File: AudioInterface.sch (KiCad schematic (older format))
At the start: 2 parts, among them J3 Conn_01x03_Male

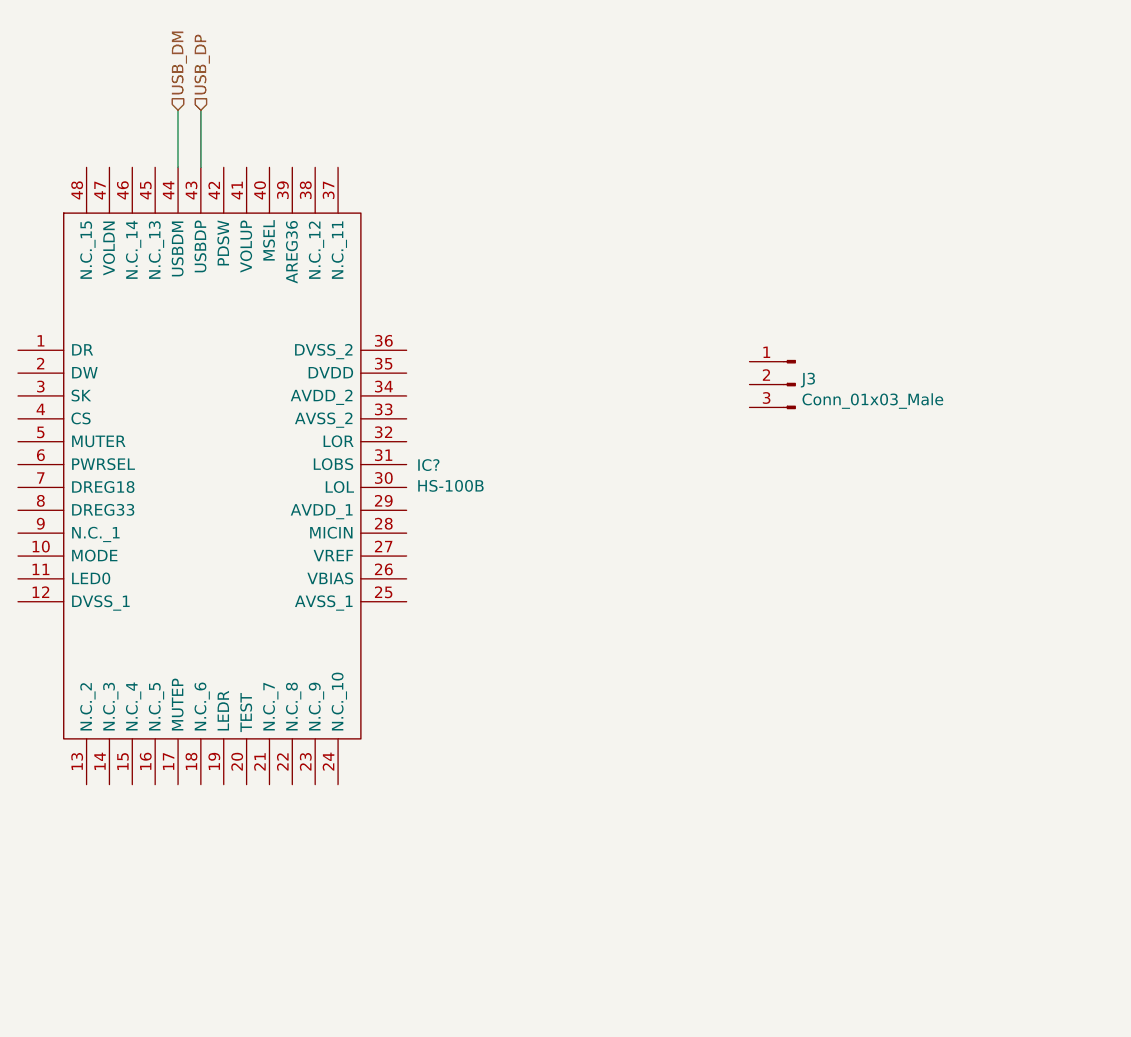
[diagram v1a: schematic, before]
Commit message: First pass at audio
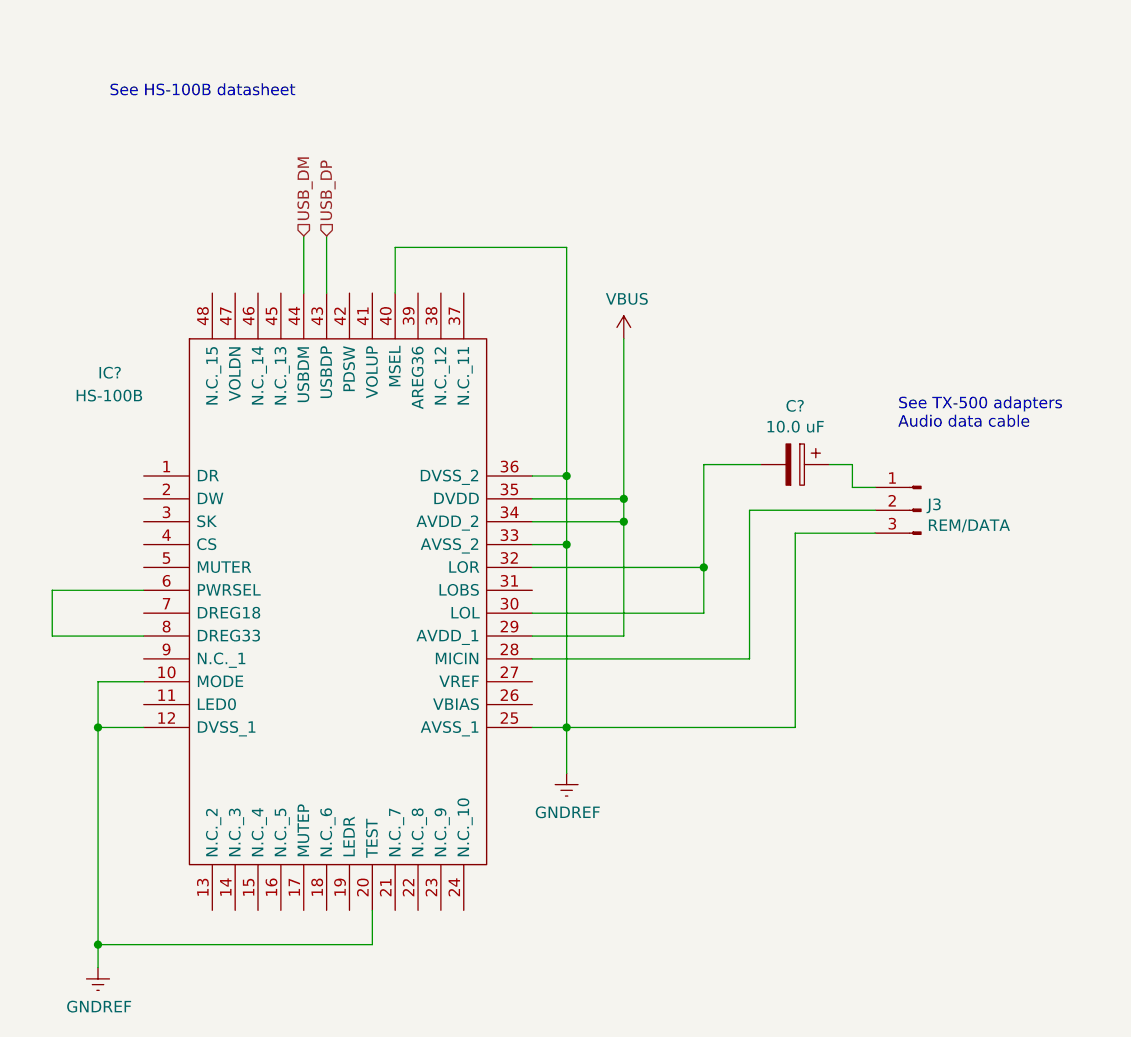
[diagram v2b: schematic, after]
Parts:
- added C?: 10.0 uF, symbol Device:CP
- J3: value Conn_01x03_Male -> REM/DATA
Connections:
- net GNDREF: now reaches IC?.10 (MODE)
- net GNDREF: now also IC?.12 (DVSS_1), IC?.20 (TEST), IC?.25 (AVSS_1), IC?.33 (AVSS_2), IC?.36 (DVSS_2), IC?.40 (MSEL), J3.3 (Pin_3)
- net at IC?.28 (MICIN): now also J3.2 (Pin_2)
- net VBUS: now reaches IC?.29 (AVDD_1)
- net VBUS: now also IC?.34 (AVDD_2), IC?.35 (DVDD)
- net at IC?.30 (LOL): now also IC?.32 (LOR), C?.2
- net at IC?.6 (PWRSEL): now also IC?.8 (DREG33)
- net at J3.1 (Pin_1): now also C?.1
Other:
- note added: "See HS-100B datasheet"
- note added: "See TX-500 adapters\nAudio data cable"
- moved on the sheet: IC?, J3
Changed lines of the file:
@@
 $Descr A4 11693 8268
 encoding utf-8
-Sheet 4 6
+Sheet 3 6
 Title ""
 Date ""
@@
 L HS-100B:HS-100B IC?
 U 1 1 605AF753
-P 4250 2800
+P 4800 3350
 AR Path="/605AF753" Ref="IC?"  Part="1"
 AR Path="/605AB33C/605AF753" Ref="IC?"  Part="1"
-F 0 "IC?" H 5994 2296 50  0000 L CNN
-F 1 "HS-100B" H 5994 2205 50  0000 L CNN
-F 2 "QFP50P900X900X160-48N" H 5800 3400 50  0001 L CNN
-F 3 "https://datasheet.lcsc.com/szlcsc/1906061502_Cmedia-HS-100B_C371351.pdf" H 5800 3300 50  0001 L CNN
-F 4 "LQFP-48 Video-Audio Interface ICs RoHS" H 5800 3200 50  0001 L CNN "Description"
-F 5 "1.6" H 5800 3100 50  0001 L CNN "Height"
-F 6 "cmedia" H 5800 3000 50  0001 L CNN "Manufacturer_Name"
-F 7 "HS-100B" H 5800 2900 50  0001 L CNN "Manufacturer_Part_Number"
-F 8 "" H 5800 2800 50  0001 L CNN "Mouser Part Number"
-F 9 "" H 5800 2700 50  0001 L CNN "Mouser Price/Stock"
-F 10 "" H 5800 2600 50  0001 L CNN "Arrow Part Number"
-F 11 "" H 5800 2500 50  0001 L CNN "Arrow Price/Stock"
-	1    4250 2800
+F 0 "IC?" H 4600 3800 50  0000 L CNN
+F 1 "HS-100B" H 4500 3700 50  0000 L CNN
+F 2 "QFP50P900X900X160-48N" H 6350 3950 50  0001 L CNN
+F 3 "https://datasheet.lcsc.com/szlcsc/1906061502_Cmedia-HS-100B_C371351.pdf" H 6350 3850 50  0001 L CNN
+F 4 "LQFP-48 Video-Audio Interface ICs RoHS" H 6350 3750 50  0001 L CNN "Description"
+F 5 "1.6" H 6350 3650 50  0001 L CNN "Height"
+F 6 "cmedia" H 6350 3550 50  0001 L CNN "Manufacturer_Name"
+F 7 "HS-100B" H 6350 3450 50  0001 L CNN "Manufacturer_Part_Number"
+F 8 "" H 6350 3350 50  0001 L CNN "Mouser Part Number"
+F 9 "" H 6350 3250 50  0001 L CNN "Mouser Price/Stock"
+F 10 "" H 6350 3150 50  0001 L CNN "Arrow Part Number"
+F 11 "" H 6350 3050 50  0001 L CNN "Arrow Price/Stock"
+	1    4800 3350
 	1    0    0    -1
 $EndComp
@@
 L Connector:Conn_01x03_Male J?
 U 1 1 605AF759
-P 7650 2950
+P 8200 3500
 AR Path="/605AF759" Ref="J?"  Part="1"
 AR Path="/605AB33C/605AF759" Ref="J3"  Part="1"
-F 0 "J3" H 7622 2974 50  0000 R CNN
-F 1 "Conn_01x03_Male" H 7622 2883 50  0000 R CNN
-F 2 "" H 7650 2950 50  0001 C CNN
-F 3 "~" H 7650 2950 50  0001 C CNN
-	1    7650 2950
+F 0 "J3" H 8172 3524 50  0000 R CNN
+F 1 "REM/DATA" H 8172 3433 50  0000 R CNN
+F 2 "" H 8200 3500 50  0001 C CNN
+F 3 "~" H 8200 3500 50  0001 C CNN
+	1    8200 3500
 	-1   0    0    -1
 $EndComp
-Text HLabel 5050 1750 1    50   Input ~ 0
+Text HLabel 5600 2300 1    50   Input ~ 0
 USB_DP
-Text HLabel 4950 1750 1    50   Input ~ 0
+Text HLabel 5500 2300 1    50   Input ~ 0
 USB_DM
 Wire Wire Line
-	5050 1750 5050 2000
+	5600 2300 5600 2550
 Wire Wire Line
-	4950 1750 4950 2000
+	5500 2300 5500 2550
+$Comp
+L power:GNDREF #PWR?
+U 1 1 604B503B
+P 6650 4650
+F 0 "#PWR?" H 6650 4400 50  0001 C CNN
+F 1 "GNDREF" H 6655 4477 50  0000 C CNN
+F 2 "" H 6650 4650 50  0001 C CNN
+F 3 "" H 6650 4650 50  0001 C CNN
+	1    6650 4650
+	1    0    0    -1
+$EndComp
+Wire Wire Line
+	6500 3350 6650 3350
+Wire Wire Line
+	6650 3350 6650 3650
+Wire Wire Line
+	6500 3650 6650 3650
+Connection ~ 6650 3650
+Wire Wire Line
+	6650 3650 6650 4450
+Wire Wire Line
+	6500 4450 6650 4450
+Connection ~ 6650 4450
+Wire Wire Line
+	6650 4450 6650 4650
+$Comp
+L power:GNDREF #PWR?
+U 1 1 604B77F8
+P 4600 5500
+F 0 "#PWR?" H 4600 5250 50  0001 C CNN
+F 1 "GNDREF" H 4605 5327 50  0000 C CNN
+F 2 "" H 4600 5500 50  0001 C CNN
+F 3 "" H 4600 5500 50  0001 C CNN
+	1    4600 5500
+	1    0    0    -1
+$EndComp
+Wire Wire Line
+	4800 4450 4600 4450
+Wire Wire Line
+	6500 4150 7450 4150
+Wire Wire Line
+	7450 4150 7450 3500
+Wire Wire Line
+	7450 3500 8000 3500
+Wire Wire Line
+	6500 3950 7250 3950
+Wire Wire Line
+	7250 3950 7250 3750
+Wire Wire Line
+	6500 3750 7250 3750
+Connection ~ 7250 3750
+$Comp
+L power:VBUS #PWR?
+U 1 1 604B97A3
+P 6900 2750
+F 0 "#PWR?" H 6900 2600 50  0001 C CNN
+F 1 "VBUS" H 6915 2923 50  0000 C CNN
+F 2 "" H 6900 2750 50  0001 C CNN
+F 3 "" H 6900 2750 50  0001 C CNN
+	1    6900 2750
+	1    0    0    -1
+$EndComp
+Wire Wire Line
+	6500 3450 6900 3450
+Wire Wire Line
+	6900 3450 6900 2750
+Wire Wire Line
+	6500 3550 6900 3550
+Wire Wire Line
+	6900 3550 6900 3450
+Connection ~ 6900 3450
+Wire Wire Line
+	6500 4050 6900 4050
+Wire Wire Line
+	6900 4050 6900 3550
+Connection ~ 6900 3550
+Wire Wire Line
+	5800 5250 5800 5400
+Wire Wire Line
+	5800 5400 4600 5400
+Wire Wire Line
+	4600 4450 4600 5400
+Wire Wire Line
+	4600 5400 4600 5500
+Connection ~ 4600 5400
+Wire Wire Line
+	4800 4250 4600 4250
+Wire Wire Line
+	4600 4250 4600 4450
+Connection ~ 4600 4450
+Wire Wire Line
+	4800 4050 4400 4050
+Wire Wire Line
+	4400 4050 4400 3850
+Wire Wire Line
+	4400 3850 4800 3850
+Wire Wire Line
+	5900 2550 5900 2350
+Wire Wire Line
+	5900 2350 6650 2350
+Wire Wire Line
+	6650 2350 6650 3350
+Connection ~ 6650 3350
+Text Notes 4650 1700 0    50   ~ 0
+See HS-100B datasheet
+Text Notes 8100 3150 0    50   ~ 0
+See TX-500 adapters\nAudio data cable
+$Comp
+L Device:CP C?
+U 1 1 604CC1E1
+P 7650 3300
+F 0 "C?" V 7395 3300 50  0000 C CNN
+F 1 "10.0 uF" V 7486 3300 50  0000 C CNN
+F 2 "" H 7688 3150 50  0001 C CNN
+F 3 "~" H 7650 3300 50  0001 C CNN
+	1    7650 3300
+	0    1    1    0
+$EndComp
+Wire Wire Line
+	7250 3300 7500 3300
+Wire Wire Line
+	7250 3300 7250 3750
+Wire Wire Line
+	7800 3300 7900 3300
+Wire Wire Line
+	7900 3300 7900 3400
+Wire Wire Line
+	7900 3400 8000 3400
+Wire Wire Line
+	8000 3600 7650 3600
+Wire Wire Line
+	7650 3600 7650 4450
+Wire Wire Line
+	7650 4450 6650 4450
 $EndSCHEMATC

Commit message: First pass at pcb layout
Not really ready to set that in stone, but wanted to get an idea of what size enclosure will work.
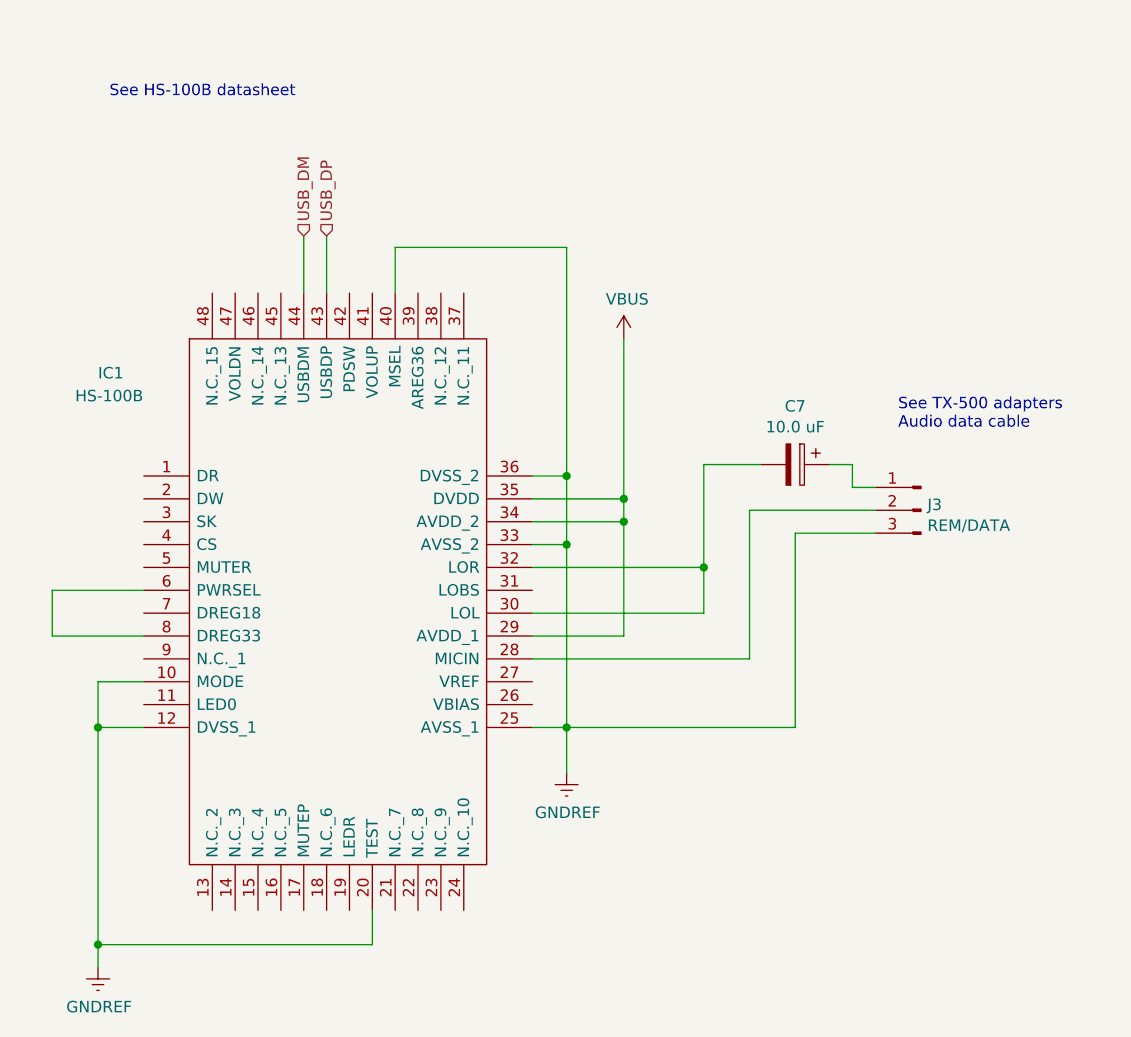
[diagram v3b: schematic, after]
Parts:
- C7: renamed from C?; footprint (none) -> Capacitor_SMD:CP_Elec_4x3
- IC1: renamed from IC?; footprint QFP50P900X900X160-48N -> Package_QFP:LQFP-48_7x7mm_P0.5mm
- J3: footprint (none) -> Connector_JST:JST_PH_B3B-PH-SM4-TB_1x03-1MP_P2.00mm_Vertical
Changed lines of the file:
@@
 P 4800 3350
 AR Path="/605AF753" Ref="IC?"  Part="1"
-AR Path="/605AB33C/605AF753" Ref="IC?"  Part="1"
-F 0 "IC?" H 4600 3800 50  0000 L CNN
+AR Path="/605AB33C/605AF753" Ref="IC1"  Part="1"
+F 0 "IC1" H 4600 3800 50  0000 L CNN
 F 1 "HS-100B" H 4500 3700 50  0000 L CNN
-F 2 "QFP50P900X900X160-48N" H 6350 3950 50  0001 L CNN
+F 2 "Package_QFP:LQFP-48_7x7mm_P0.5mm" H 6350 3950 50  0001 L CNN
 F 3 "https://datasheet.lcsc.com/szlcsc/1906061502_Cmedia-HS-100B_C371351.pdf" H 6350 3850 50  0001 L CNN
 F 4 "LQFP-48 Video-Audio Interface ICs RoHS" H 6350 3750 50  0001 L CNN "Description"
@@
 F 0 "J3" H 8172 3524 50  0000 R CNN
 F 1 "REM/DATA" H 8172 3433 50  0000 R CNN
-F 2 "" H 8200 3500 50  0001 C CNN
+F 2 "Connector_JST:JST_PH_B3B-PH-SM4-TB_1x03-1MP_P2.00mm_Vertical" H 8200 3500 50  0001 C CNN
 F 3 "~" H 8200 3500 50  0001 C CNN
 	1    8200 3500
@@
 	5500 2300 5500 2550
 $Comp
-L power:GNDREF #PWR?
+L power:GNDREF #PWR0110
 U 1 1 604B503B
 P 6650 4650
-F 0 "#PWR?" H 6650 4400 50  0001 C CNN
+F 0 "#PWR0110" H 6650 4400 50  0001 C CNN
 F 1 "GNDREF" H 6655 4477 50  0000 C CNN
 F 2 "" H 6650 4650 50  0001 C CNN
@@
 	6650 4450 6650 4650
 $Comp
-L power:GNDREF #PWR?
+L power:GNDREF #PWR0111
 U 1 1 604B77F8
 P 4600 5500
-F 0 "#PWR?" H 4600 5250 50  0001 C CNN
+F 0 "#PWR0111" H 4600 5250 50  0001 C CNN
 F 1 "GNDREF" H 4605 5327 50  0000 C CNN
 F 2 "" H 4600 5500 50  0001 C CNN
@@
 Connection ~ 7250 3750
 $Comp
-L power:VBUS #PWR?
+L power:VBUS #PWR0112
 U 1 1 604B97A3
 P 6900 2750
-F 0 "#PWR?" H 6900 2600 50  0001 C CNN
+F 0 "#PWR0112" H 6900 2600 50  0001 C CNN
 F 1 "VBUS" H 6915 2923 50  0000 C CNN
 F 2 "" H 6900 2750 50  0001 C CNN
@@
 See TX-500 adapters\nAudio data cable
 $Comp
-L Device:CP C?
+L Device:CP C7
 U 1 1 604CC1E1
 P 7650 3300
-F 0 "C?" V 7395 3300 50  0000 C CNN
+F 0 "C7" V 7395 3300 50  0000 C CNN
 F 1 "10.0 uF" V 7486 3300 50  0000 C CNN
-F 2 "" H 7688 3150 50  0001 C CNN
+F 2 "Capacitor_SMD:CP_Elec_4x3" H 7688 3150 50  0001 C CNN
 F 3 "~" H 7650 3300 50  0001 C CNN
 	1    7650 3300

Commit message: Swap TUSB4041I for TUSB2036
The 4041 does more than I need it to, so use the 2036 instead.
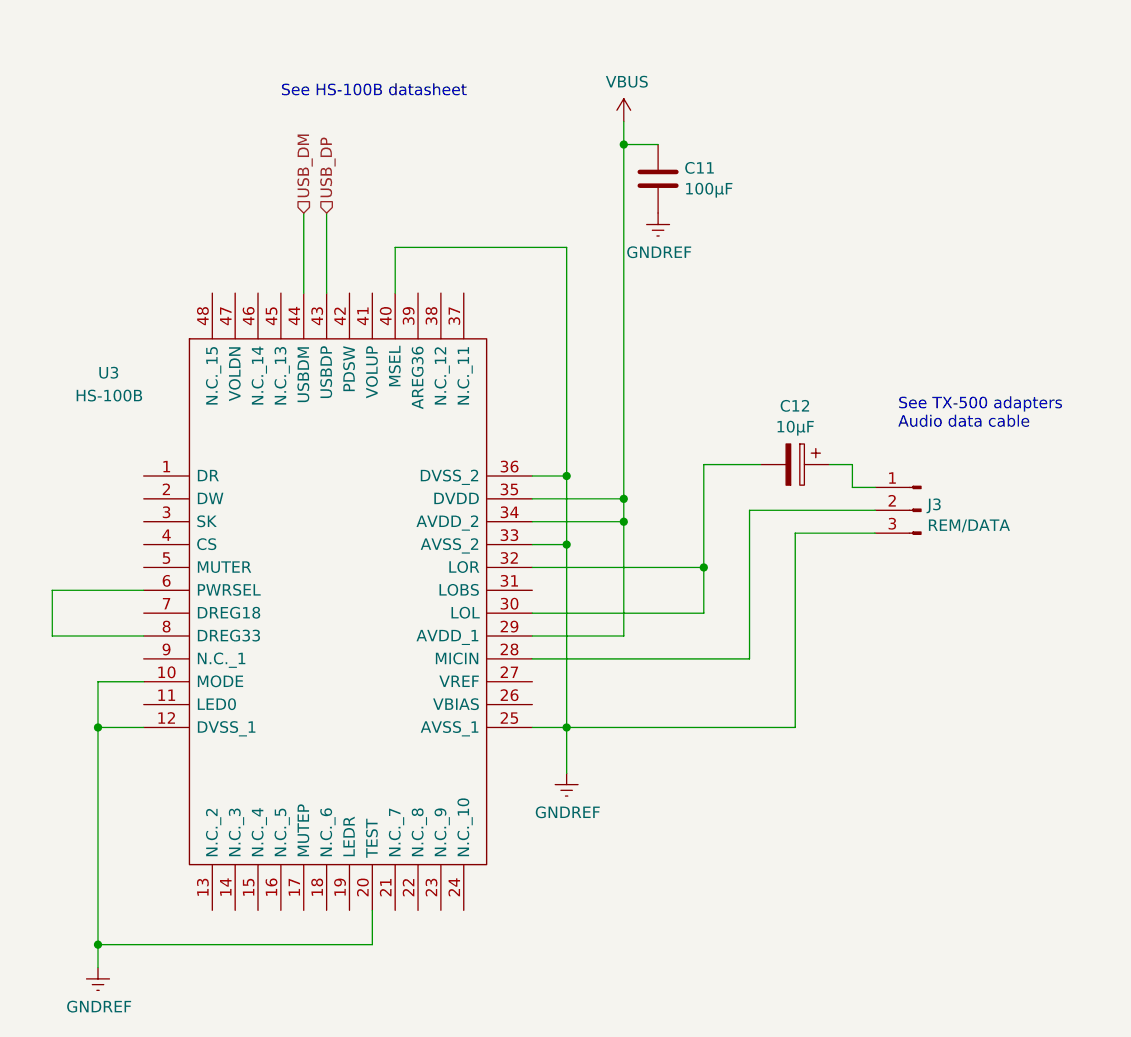
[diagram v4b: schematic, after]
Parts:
- added C11: 100μF, Capacitor_SMD:CP_Elec_4x3, symbol Device:C
- C12: renamed from C7; value 10.0 uF -> 10μF
- renumbered IC1 to U3
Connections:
- net GNDREF: now also C11.2
- net VBUS: now also C11.1
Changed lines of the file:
@@
 P 4800 3350
 AR Path="/605AF753" Ref="IC?"  Part="1"
-AR Path="/605AB33C/605AF753" Ref="IC1"  Part="1"
-F 0 "IC1" H 4600 3800 50  0000 L CNN
+AR Path="/605AB33C/605AF753" Ref="U3"  Part="1"
+F 0 "U3" H 4600 3800 50  0000 L CNN
 F 1 "HS-100B" H 4500 3700 50  0000 L CNN
 F 2 "Package_QFP:LQFP-48_7x7mm_P0.5mm" H 6350 3950 50  0001 L CNN
@@
 	-1   0    0    -1
 $EndComp
-Text HLabel 5600 2300 1    50   Input ~ 0
-USB_DP
-Text HLabel 5500 2300 1    50   Input ~ 0
-USB_DM
-Wire Wire Line
-	5600 2300 5600 2550
-Wire Wire Line
-	5500 2300 5500 2550
 $Comp
 L power:GNDREF #PWR0110
@@
 L power:VBUS #PWR0112
 U 1 1 604B97A3
-P 6900 2750
-F 0 "#PWR0112" H 6900 2600 50  0001 C CNN
-F 1 "VBUS" H 6915 2923 50  0000 C CNN
-F 2 "" H 6900 2750 50  0001 C CNN
-F 3 "" H 6900 2750 50  0001 C CNN
-	1    6900 2750
+P 6900 1800
+F 0 "#PWR0112" H 6900 1650 50  0001 C CNN
+F 1 "VBUS" H 6915 1973 50  0000 C CNN
+F 2 "" H 6900 1800 50  0001 C CNN
+F 3 "" H 6900 1800 50  0001 C CNN
+	1    6900 1800
 	1    0    0    -1
 $EndComp
@@
 	6500 3450 6900 3450
 Wire Wire Line
-	6900 3450 6900 2750
-Wire Wire Line
 	6500 3550 6900 3550
 Wire Wire Line
 	6900 3550 6900 3450
-Connection ~ 6900 3450
 Wire Wire Line
 	6500 4050 6900 4050
@@
 	6650 2350 6650 3350
 Connection ~ 6650 3350
-Text Notes 4650 1700 0    50   ~ 0
+Text Notes 5400 1700 0    50   ~ 0
 See HS-100B datasheet
 Text Notes 8100 3150 0    50   ~ 0
 See TX-500 adapters\nAudio data cable
 $Comp
-L Device:CP C7
+L Device:CP C12
 U 1 1 604CC1E1
 P 7650 3300
-F 0 "C7" V 7395 3300 50  0000 C CNN
-F 1 "10.0 uF" V 7486 3300 50  0000 C CNN
+F 0 "C12" V 7395 3300 50  0000 C CNN
+F 1 "10μF" V 7486 3300 50  0000 C CNN
 F 2 "Capacitor_SMD:CP_Elec_4x3" H 7688 3150 50  0001 C CNN
 F 3 "~" H 7650 3300 50  0001 C CNN
@@
 Wire Wire Line
 	7650 4450 6650 4450
+Text HLabel 5600 2200 1    50   Input ~ 0
+USB_DP
+Text HLabel 5500 2200 1    50   Input ~ 0
+USB_DM
+$Comp
+L Device:C C11
+U 1 1 605433B2
+P 7050 2050
+F 0 "C11" H 7165 2096 50  0000 L CNN
+F 1 "100μF" H 7165 2005 50  0000 L CNN
+F 2 "Capacitor_SMD:CP_Elec_4x3" H 7088 1900 50  0001 C CNN
+F 3 "~" H 7050 2050 50  0001 C CNN
+	1    7050 2050
+	1    0    0    -1
+$EndComp
+Wire Wire Line
+	7050 1900 6900 1900
+Connection ~ 6900 1900
+Wire Wire Line
+	6900 1900 6900 1800
+$Comp
+L power:GNDREF #PWR0129
+U 1 1 60544A17
+P 7050 2200
+F 0 "#PWR0129" H 7050 1950 50  0001 C CNN
+F 1 "GNDREF" H 7055 2027 50  0000 C CNN
+F 2 "" H 7050 2200 50  0001 C CNN
+F 3 "" H 7050 2200 50  0001 C CNN
+	1    7050 2200
+	1    0    0    -1
+$EndComp
+Wire Wire Line
+	6900 1900 6900 3450
+Connection ~ 6900 3450
+Wire Wire Line
+	5600 2200 5600 2550
+Wire Wire Line
+	5500 2200 5500 2550
 $EndSCHEMATC
